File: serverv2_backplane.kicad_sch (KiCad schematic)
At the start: 4 parts, among them CN3 H2541FV-C762-2X04P, U11 TPS65987DDJRSHR

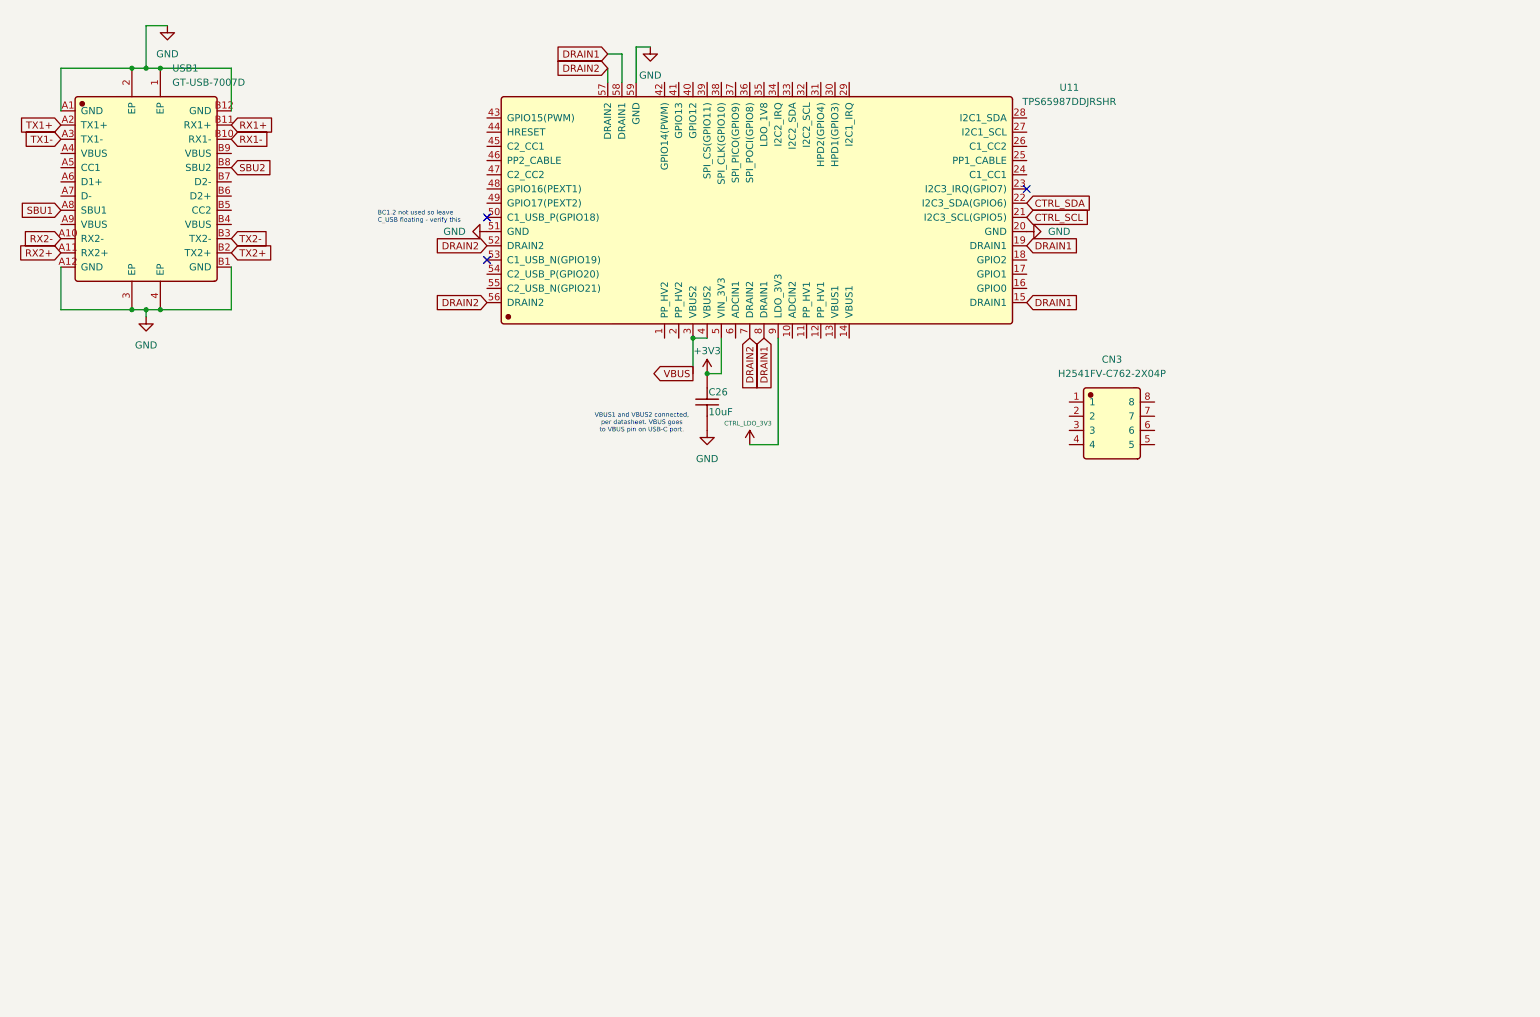
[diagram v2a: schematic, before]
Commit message: Preliminary draft of USB controller and power circuit
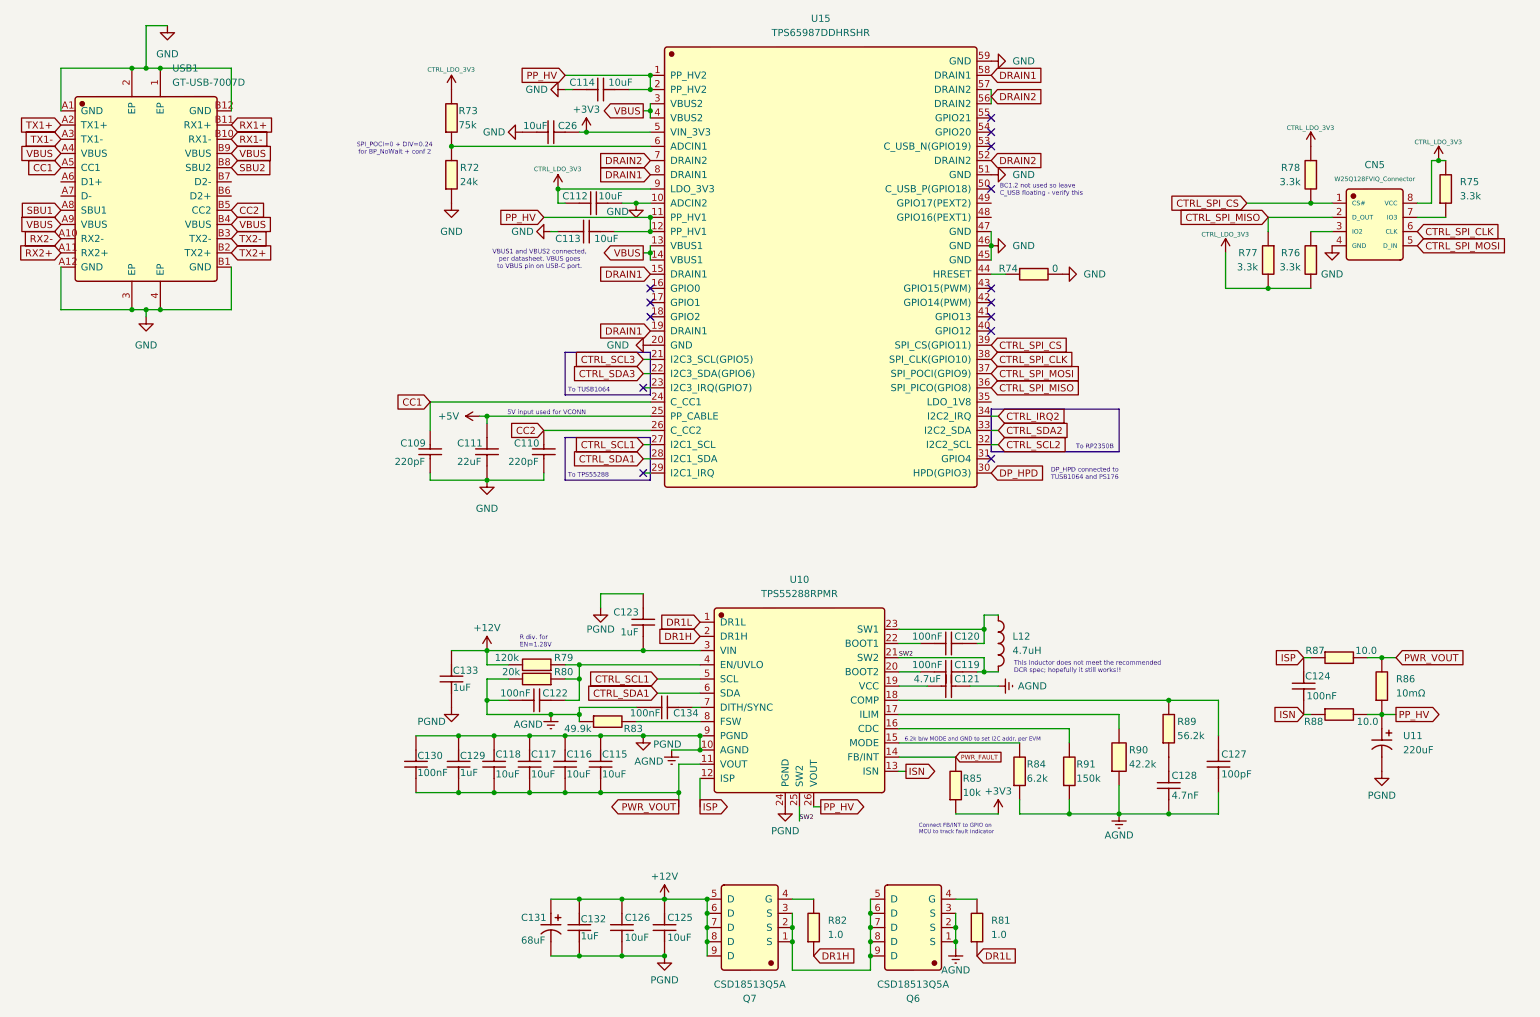
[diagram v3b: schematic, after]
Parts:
- removed CN3: H2541FV-C762-2X04P, JLCImport:H2541FV-C762-2X04P, symbol JLCImport:H2541FV-C762-2X04P
- removed U11: TPS65987DDJRSHR, JLCImport:TPS65987DDJRSHR, symbol JLCImport:TPS65987DDJRSHR
- added C109, C110: 220pF, Capacitor_SMD:C_0402_1005Metric, symbol JLCImport:0402B221K500NT
- added C111: 22uF, Capacitor_SMD:C_0603_1608Metric, symbol JLCImport:CL10A226MQ8NRNC
- added C112: 10uF, Capacitor_SMD:C_0603_1608Metric, symbol JLCImport:CL10A106KP8NNNC
- added C113, C114, C115, C116, C117, C118, C125, C126: 10uF, Capacitor_SMD:C_0805_2012Metric, symbol JLCImport:CL21A106KAYNNNE
- added C119, C120, C122, C124, C130, C134: 100nF, Capacitor_SMD:C_0402_1005Metric, symbol JLCImport:CL05B104KB54PNC
- added C121: 4.7uF, Capacitor_SMD:C_0805_2012Metric, symbol JLCImport:CL21A475KAQNNNE
- added C123: 1uF, Capacitor_SMD:C_0603_1608Metric, symbol JLCImport:CL10A105KB8NNNC
- added C127: 100pF, Capacitor_SMD:C_0402_1005Metric, symbol JLCImport:TCC0402COG101J101AT
- added C128: 4.7nF, Capacitor_SMD:C_0402_1005Metric, symbol JLCImport:CGA0402X7R472K250GT
- added C129, C132, C133: 1uF, Capacitor_SMD:C_0402_1005Metric, symbol JLCImport:CL05A105KA5NQNC
- added C131: 68uF, JLCImport:DHG100M686G150S1AA, symbol JLCImport:DHG100M686G150S1AA
- added CN5: W25Q128FVIQ_Connector, JLCImport:H2541FV-C762-2X04P, symbol JLCImport:H2541FV-C762-2X04P
- added L12: 4.7uH, JLCImport:SL1040-4R7M, symbol JLCImport:SL1040-4R7M
- added Q6, Q7: CSD18513Q5A, JLCImport:CSD18513Q5A, symbol JLCImport:CSD18513Q5A
- added R72: 24k, Resistor_SMD:R_0603_1608Metric, symbol JLCImport:0603WAF2402T5E
- added R73: 75k, Resistor_SMD:R_0603_1608Metric, symbol JLCImport:0603WAF7502T5E
- added R74: 0, Resistor_SMD:R_0402_1005Metric, symbol JLCImport:0402WGF0000TCE
- added R75, R76, R77, R78: 3.3k, Resistor_SMD:R_0402_1005Metric, symbol JLCImport:0402WGF3301TCE
- added R79: 120k, Resistor_SMD:R_0603_1608Metric, symbol JLCImport:0603WAF1203T5E
- added R80: 20k, Resistor_SMD:R_0402_1005Metric, symbol JLCImport:0402WGF2002TCE
- added R81, R82: 1.0, Resistor_SMD:R_0402_1005Metric, symbol JLCImport:WR04W1R00FTL
- added R83: 49.9k, Resistor_SMD:R_0402_1005Metric, symbol JLCImport:RMS04FT4992
- added R84: 6.2k, Resistor_SMD:R_0603_1608Metric, symbol JLCImport:0603WAF6201T5E
- added R85: 10k, Resistor_SMD:R_0402_1005Metric, symbol JLCImport:0402WGF1002TCE
- added R86: 10mΩ, Resistor_SMD:R_1206_3216Metric, symbol JLCImport:1206W3J010LT5E
- added R87, R88: 10.0, Resistor_SMD:R_0402_1005Metric, symbol JLCImport:0402WGF100JTCE
- added R89: 56.2k, Resistor_SMD:R_0402_1005Metric, symbol JLCImport:0402WGF5622TCE
- added R90: 42.2k, Resistor_SMD:R_0402_1005Metric, symbol JLCImport:CR0402F42K2Q10Z
- added R91: 150k, Resistor_SMD:R_0603_1608Metric, symbol JLCImport:0603WAF1503T5E
- added U10: TPS55288RPMR, JLCImport:TPS55288RPMR, symbol JLCImport:TPS55288RPMR
- added U11: 220uF, TerminalBlock_Phoenix:TerminalBlock_Phoenix_PTSM-0,5-2-2.5-V-THR_1x02_P2.50mm_Vertical, symbol JLCImport:CD110227M1E0612VFL
- added U15: TPS65987DDHRSHR, Package_DFN_QFN:VQFN-40-1EP_5x5mm_P0.4mm_EP3.3x3.3mm, symbol JLCImport:TPS65987DDHRSHR
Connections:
- net +3V3: now also R85.1, U15.5 (VIN_3V3)
- net CTRL_LDO_3V3: now also C112.2, CN5.8 (VCC), R73.2, R75.2, R76.2, R77.2, R78.1, U15.9 (LDO_3V3)
- net DRAIN1: now also U15.15 (DRAIN1), U15.19 (DRAIN1), U15.58 (DRAIN1), U15.8 (DRAIN1)
- net DRAIN2: now also U15.52 (DRAIN2), U15.56 (DRAIN2), U15.57 (DRAIN2), U15.7 (DRAIN2)
- net GND: now also C109.1, C110.1, C111.1, C112.1, C113.2, C114.2, CN5.4 (GND), R72.1, R74.2, U15.10 (ADCIN2), U15.20 (GND), U15.45 (GND), U15.46 (GND), U15.47 (GND), U15.51 (GND), U15.59 (GND)
- net VBUS: now also USB1.A4 (VBUS), USB1.A9 (VBUS), USB1.B4 (VBUS), USB1.B9 (VBUS), U15.13 (VBUS1), U15.14 (VBUS1), U15.3 (VBUS2), U15.4 (VBUS2)
- net CC1: now reaches USB1.A5 (CC1)
- net CC1: now also C109.2, U15.24 (C_CC1)
- net CC2: now reaches USB1.B5 (CC2)
- net CC2: now also C110.2, U15.26 (C_CC2)
- new net: R74.1, U15.44 (HRESET)
- new net: R72.2, R73.1, U15.6 (ADCIN1)
- new net: C122.2, R79.1, R80.1, U10.4 (EN/UVLO)
- new net: C127.2, R89.2, U10.18 (COMP)
- new net: Q7.4 (G), R82.2
- new net: R84.2, U10.15 (MODE)
- new net: R91.2, U10.16 (CDC)
- new net: R90.2, U10.17 (ILIM)
- new net: C121.2, U10.19 (VCC)
- new net: C119.1, U10.20 (BOOT2)
- new net: C120.1, U10.22 (BOOT1)
- new net: C120.2, L12.1, U10.23 (SW1)
- new net: C134.2, U10.7 (DITH/SYNC)
- new net: R83.2, U10.8 (FSW)
- new net: C128.2, R89.1
- new net: CN5.7 (IO3), R75.1
- new net: Q6.4 (G), R81.2
- new net: Q6.5 (D), Q6.6 (D), Q6.7 (D), Q6.8 (D), Q6.9 (D), Q7.1 (S), Q7.2 (S), Q7.3 (S)
- new net: CN5.3 (IO2), R76.1
- new net +12V: C123.1, C125.2, C126.2, C131.1, C132.2, C133.2, Q7.5 (D), Q7.6 (D), Q7.7 (D), Q7.8 (D), Q7.9 (D), R79.2, U10.3 (VIN)
- new net +5V: C111.2, U15.25 (PP_CABLE)
- new net AGND: C115.2, C116.2, C117.2, C118.2, C121.1, C122.1, C123.2, C125.1, C126.1, C127.1, C128.1, C129.2, C130.2, C131.2, C132.1, C133.1, C134.1, Q6.1 (S), Q6.2 (S), Q6.3 (S), R80.2, R83.1, R84.1, R90.1, R91.1, U10.10 (AGND), U10.24 (PGND), U10.9 (PGND), U11.2
- new net CTRL_IRQ2: U15.34 (I2C2_IRQ)
- new net CTRL_SCL1: U10.5 (SCL), U15.27 (I2C1_SCL)
- new net CTRL_SCL2: U15.32 (I2C2_SCL)
- new net CTRL_SCL3: U15.21 (I2C3_SCL(GPIO5))
- new net CTRL_SDA1: U10.6 (SDA), U15.28 (I2C1_SDA)
- new net CTRL_SDA2: U15.33 (I2C2_SDA)
- new net CTRL_SDA3: U15.22 (I2C3_SDA(GPIO6))
- new net CTRL_SPI_CLK: CN5.6 (CLK), U15.38 (SPI_CLK(GPIO10))
- new net CTRL_SPI_CS: CN5.1 (CS#), R78.2, U15.39 (SPI_CS(GPIO11))
- new net CTRL_SPI_MISO: CN5.2 (D_OUT), R77.1, U15.36 (SPI_PICO(GPIO8))
- new net CTRL_SPI_MOSI: CN5.5 (D_IN), U15.37 (SPI_POCI(GPIO9))
- new net DP_HPD: U15.30 (HPD(GPIO3))
- new net DR1H: R82.1, U10.2 (DR1H)
- new net DR1L: R81.1, U10.1 (DR1L)
- new net ISN: C124.1, R88.1, U10.13 (ISN)
- new net ISP: C124.2, R87.1, U10.12 (ISP)
- new net PP_HV: C113.1, C114.1, R86.1, R88.2, U10.26 (VOUT), U11.1, U15.1 (PP_HV2), U15.11 (PP_HV1), U15.12 (PP_HV1), U15.2 (PP_HV2)
- new net PWR_FAULT: R85.2, U10.14 (FB/INT)
- new net PWR_VOUT: C115.1, C116.1, C117.1, C118.1, C129.1, C130.1, R86.2, R87.2, U10.11 (VOUT)
- new net SW2: C119.2, L12.2, U10.21 (SW2), U10.25 (SW2)
- no-connect marks 3 -> 14
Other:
- note added: "5V input used for VCONN"
- note added: "6.2k b/w MODE and GND to set I2C addr, per EVM"
- note added: "Connect FB/INT to GPIO on MCU to track fault indicator"
- note added: "DP_HPD connected to TUSB1064 and PS176"
- note added: "R div. for EN=1.28V"
- note added: "SPI_POCI=0 + DIV=0.24 for BP_NoWait + conf 2"
- note added: "This inductor does not meet the recommended DCR spec; hopefully it still works!!"
- note added: "To RP2350B"
- note added: "To TPS55288"
- note added: "To TUSB1064"

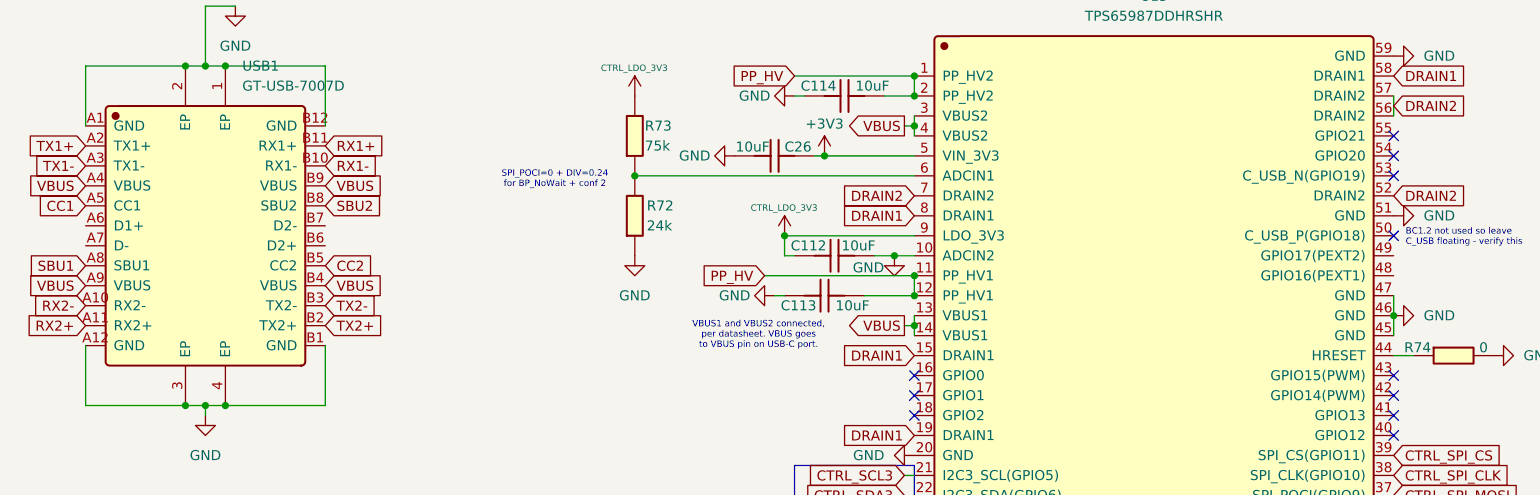
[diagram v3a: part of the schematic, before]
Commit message: Preliminary revision of USB hub and temperature monitor
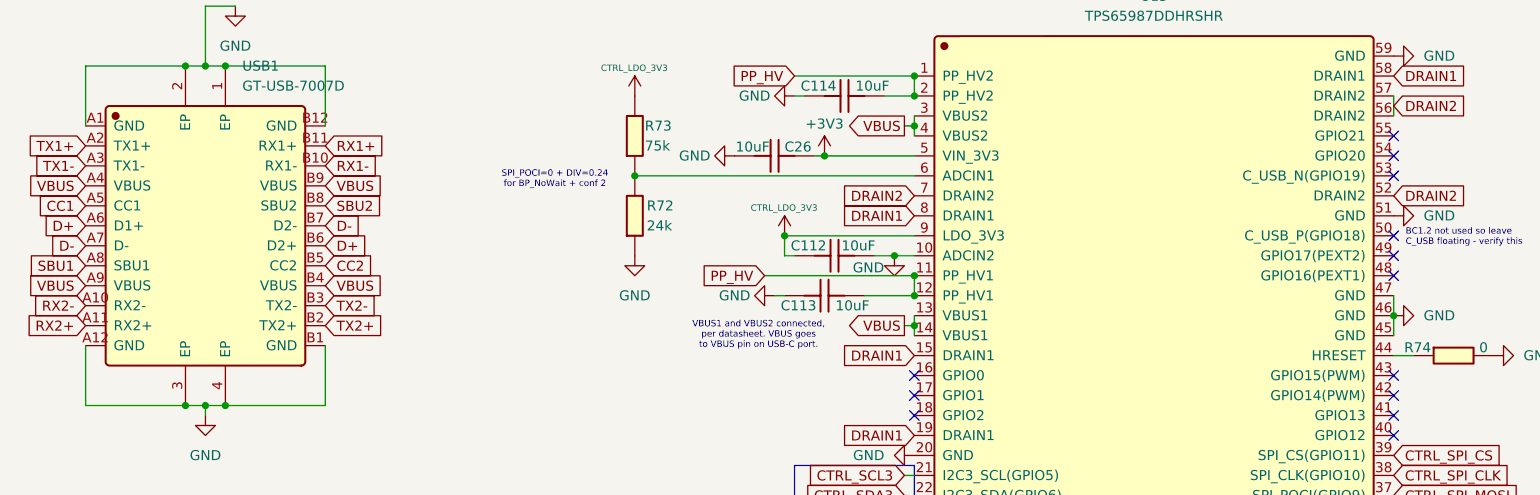
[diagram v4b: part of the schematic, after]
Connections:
- net D+: now reaches USB1.A6 (D1+)
- net D+: now also USB1.B6 (D2+)
- net D-: now reaches USB1.A7 (D-)
- net D-: now also USB1.B7 (D2-)
- no-connect marks 14 -> 16
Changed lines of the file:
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@@
+	)
+	(no_connect
+		(at 195.58 50.8)
 	)
 	(no_connect
@@
 	)
 	(no_connect
+		(at 195.58 53.34)
+	)
+	(no_connect
 		(at 195.58 68.58)
 	)
@@
 		)
 	)
+	(global_label "D-"
+		(shape input)
+		(at 29.21 49.53 180)
+		(fields_autoplaced yes)
+		(effects
+			(font
+				(size 1.27 1.27)
+			)
+			(justify right)
+		)
+		(property "Intersheetrefs" "${INTERSHEET_REFS}"
+			(at 23.3824 49.53 0)
+			(hide yes)
+			(show_name no)
+			(do_not_autoplace no)
+			(effects
+				(font
+					(size 1.27 1.27)
+				)
+				(justify right)
+			)
+		)
+	)
 	(global_label "SBU2"
 		(shape input)
@@
 				)
 				(justify right)
+			)
+		)
+	)
+	(global_label "D-"
+		(shape input)
+		(at 59.69 46.99 0)
+		(fields_autoplaced yes)
+		(effects
+			(font
+				(size 1.27 1.27)
+			)
+			(justify left)
+		)
+		(property "Intersheetrefs" "${INTERSHEET_REFS}"
+			(at 65.5176 46.99 0)
+			(hide yes)
+			(show_name no)
+			(do_not_autoplace no)
+			(effects
+				(font
+					(size 1.27 1.27)
+				)
+				(justify left)
 			)
 		)
@@
 		)
 	)
+	(global_label "D+"
+		(shape input)
+		(at 29.21 46.99 180)
+		(fields_autoplaced yes)
+		(effects
+			(font
+				(size 1.27 1.27)
+			)
+			(justify right)
+		)
+		(property "Intersheetrefs" "${INTERSHEET_REFS}"
+			(at 23.3824 46.99 0)
+			(hide yes)
+			(show_name no)
+			(do_not_autoplace no)
+			(effects
+				(font
+					(size 1.27 1.27)
+				)
+				(justify right)
+			)
+		)
+	)
 	(global_label "PWR_VOUT"
 		(shape input)
@@
 			(hide yes)
 			(show_name no)
+			(do_not_autoplace no)
+			(effects
+				(font
+					(size 1.27 1.27)
+				)
+				(justify left)
+			)
+		)
+	)
+	(global_label "D+"
+		(shape input)
+		(at 59.69 49.53 0)
+		(fields_autoplaced yes)
+		(effects
+			(font
+				(size 1.27 1.27)
+			)
+			(justify left)
+		)
+		(property "Intersheetrefs" "${INTERSHEET_REFS}"
+			(at 65.5176 49.53 0)
+			(hide yes)
+			(show_name no)
